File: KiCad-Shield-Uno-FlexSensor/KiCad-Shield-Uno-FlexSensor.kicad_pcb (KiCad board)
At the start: 2 copper layers, 68.6 x 53.3 mm, 8 parts, among them J1 Power, J2 Digital/PWM, J3 Analog, J4 Digital/PWM

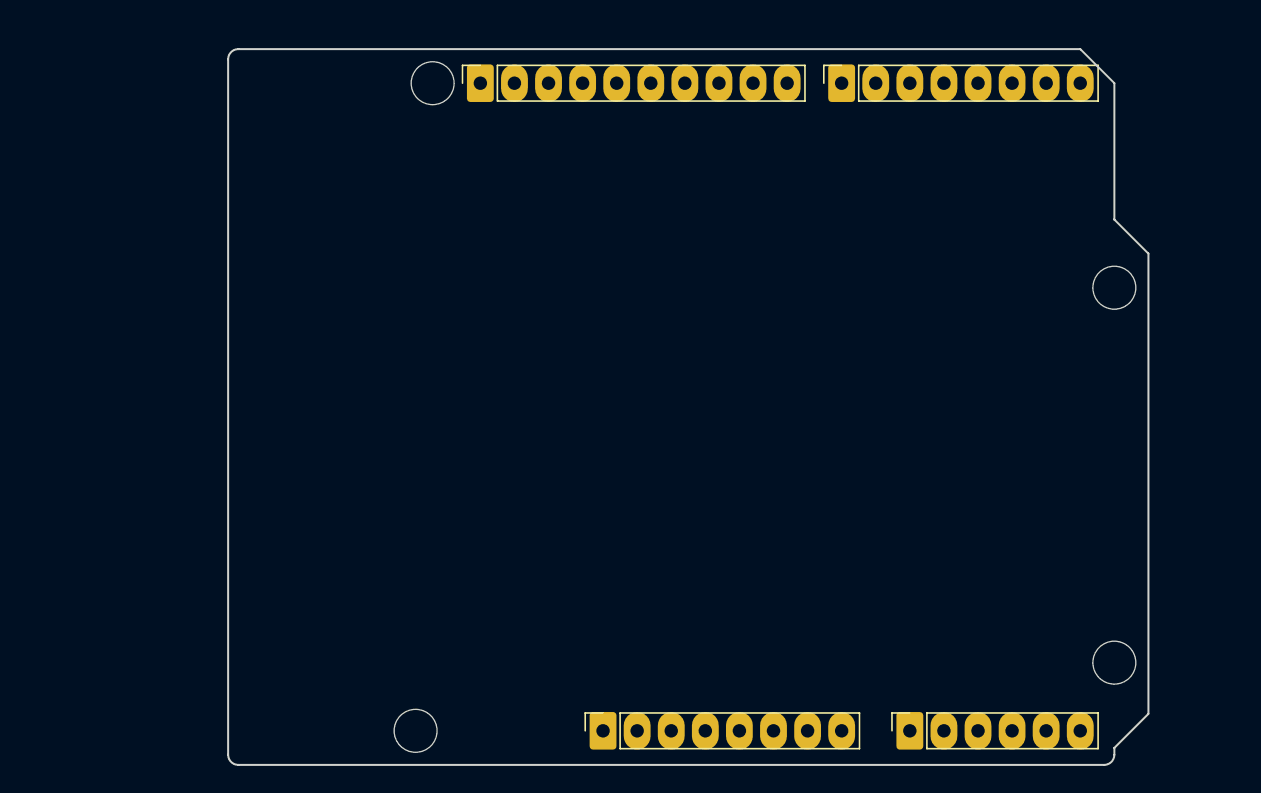
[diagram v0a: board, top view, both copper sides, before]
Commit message: Compléter le readme avec des informations complémentaires sur le cahier des charges et le matériel requis
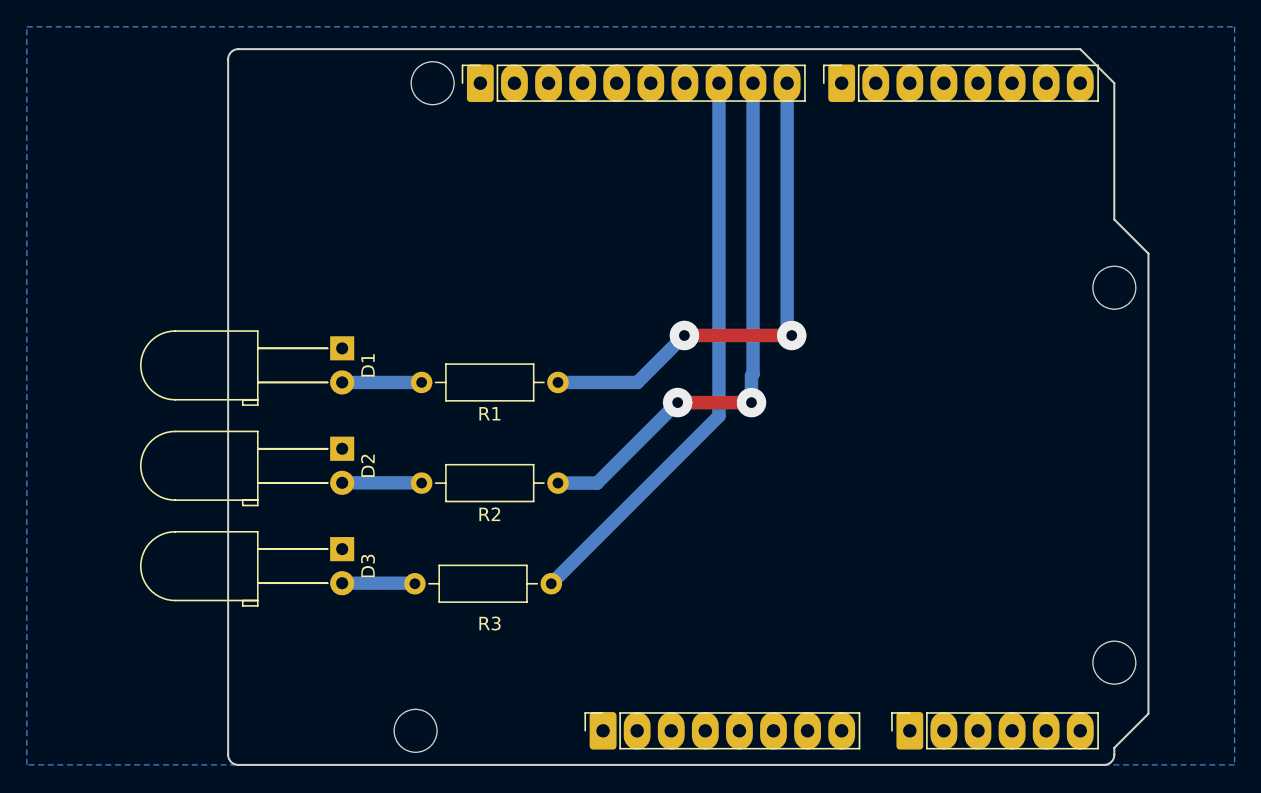
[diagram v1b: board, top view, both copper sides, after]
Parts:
- added D1: STAT, LED_THT:LED_D5.0mm_Horizontal_O6.35mm_Z3.0mm, F.Cu at (108.5, 69.0)
- added D2: MODE, LED_THT:LED_D5.0mm_Horizontal_O6.35mm_Z3.0mm, F.Cu at (108.5, 76.4)
- added D3: ERR, LED_THT:LED_D5.0mm_Horizontal_O6.35mm_Z3.0mm, F.Cu at (108.5, 83.9)
- added R1: 680, Resistor_THT:R_Axial_DIN0207_L6.3mm_D2.5mm_P10.16mm_Horizontal, F.Cu at (124.6, 71.5)
- added R2: 680, Resistor_THT:R_Axial_DIN0207_L6.3mm_D2.5mm_P10.16mm_Horizontal, F.Cu at (124.6, 79.0)
- added R3: 680, Resistor_THT:R_Axial_DIN0207_L6.3mm_D2.5mm_P10.16mm_Horizontal, F.Cu at (124.1, 86.5)
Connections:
- J2 pad 10: unconnected-(J2-Pin_10-Pad10) -> /D8
- J2 pad 7: unconnected-(J2-Pin_7-Pad7) -> /D11
- J2 pad 8: unconnected-(J2-Pin_8-Pad8) -> /D10
- J2 pad 9: unconnected-(J2-Pin_9-Pad9) -> /D9
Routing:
- net /D10: track 0.00 -> 42.5 mm
- net /D9: track 0.00 -> 40.8 mm, vias 0 -> 2
- net /D8: track 0.00 -> 37.8 mm, vias 0 -> 2
- net Net-(D2-A): track 0.00 -> 5.93 mm
- net Net-(D1-A): track 0.00 -> 5.92 mm
- net Net-(D3-A): track 0.00 -> 5.44 mm
- added copper zone on B.Cu, net GND
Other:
- board text added: "Plan de Masse"
